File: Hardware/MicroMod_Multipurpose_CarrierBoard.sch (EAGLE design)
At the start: 100 parts, among them J11 microSD, J12 SPI, J14 I2C, J16 General GPIO, J17 I2C1, J18 DAC, J19 SPI1, J20 2.4" TFT, J3 JTAG, J5 UART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

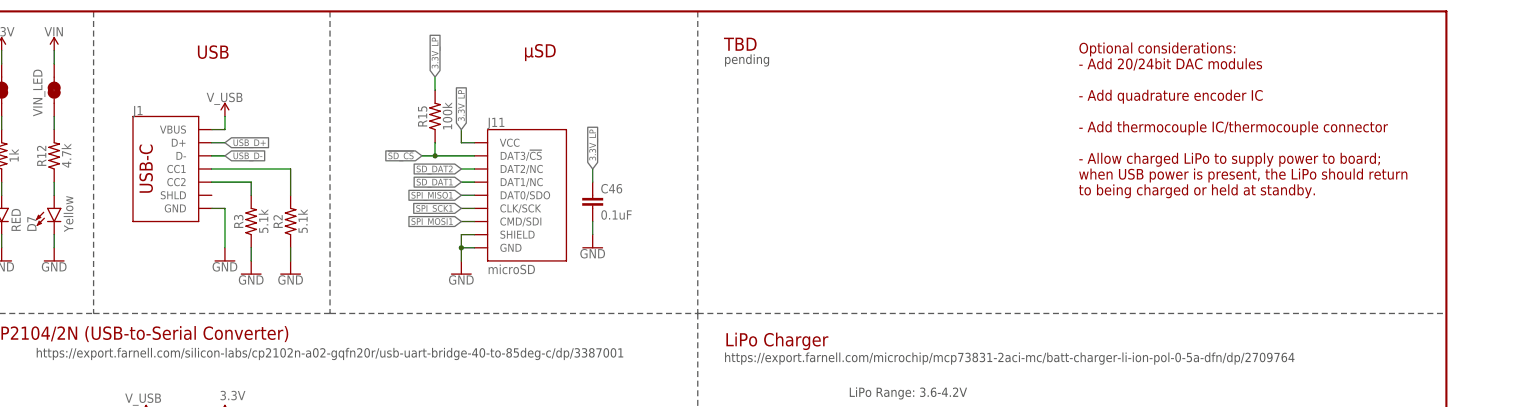
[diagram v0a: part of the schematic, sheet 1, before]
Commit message: Add ESD protection to USB data-lines
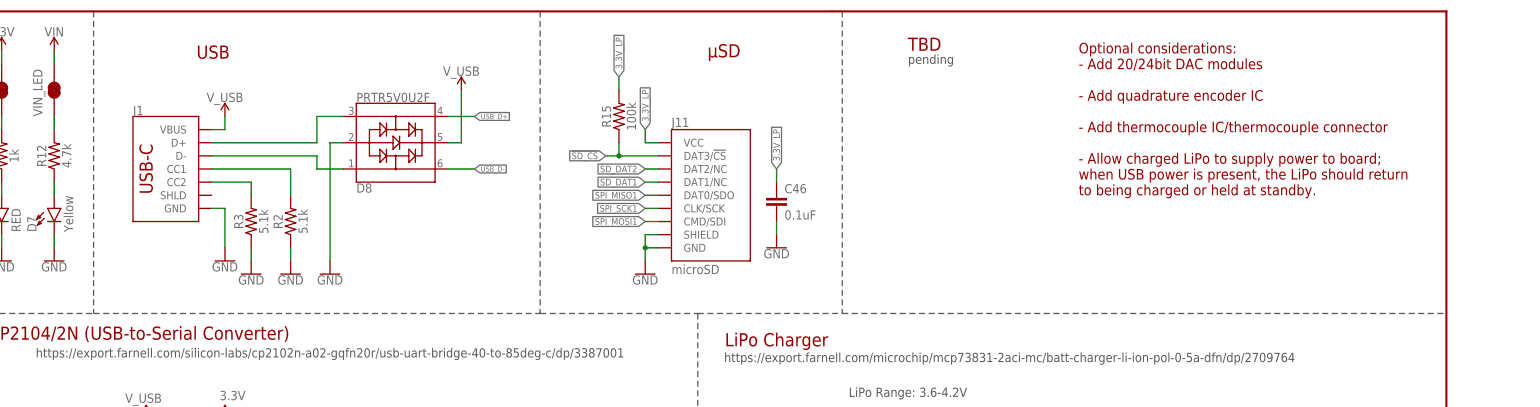
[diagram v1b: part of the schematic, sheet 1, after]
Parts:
- added D8: PRTR5V0U2F, SparkFun-IC-Power:PRTR5V0U2F
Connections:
- new net N$23: D8.1, J1.D-
- new net N$24: D8.3, J1.D+
- net GND: now also D8.2
- net USB_D+: now also D8.4; no longer J1.D+
- net USB_D-: now also D8.6; no longer J1.D-
- net V_USB: now also D8.5
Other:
- moved on the sheet: C46, J11, R15

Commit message: Minor correction
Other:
- note added: "Optional considerations: - Add 20/24bit ADC modules - Add quadrature encoder IC - Add thermocouple IC/thermocouple connector"
- note removed: "Optional considerations: - Add 20/24bit DAC modules - Add quadrature encoder IC - Add thermocouple IC/thermocouple connector - Allow charged LiPo to supply power to board; when USB power is present, the LiPo should return to being charged or held at standby."
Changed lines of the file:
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@@
 <wire x1="368.3" y1="106.68" x2="370.84" y2="106.68" width="0.2032" layer="97" style="longdash"/>
 <wire x1="370.84" y1="106.68" x2="370.84" y2="35.56" width="0.2032" layer="97" style="longdash"/>
-<text x="360.68" y="243.84" size="2.032" layer="94">Optional considerations:
-- Add 20/24bit DAC modules
+<text x="327.66" y="241.3" size="2.032" layer="94">Optional considerations:
+- Add 20/24bit ADC modules
 - Add quadrature encoder IC
 - Add thermocouple IC/thermocouple connector
-- Allow charged LiPo to supply power to board;
-when USB power is present, the LiPo should return
-to being charged or held at standby.</text>
+</text>
 <wire x1="137.16" y1="144.78" x2="132.08" y2="144.78" width="0.2032" layer="97" style="longdash"/>
 <wire x1="132.08" y1="144.78" x2="132.08" y2="124.46" width="0.2032" layer="97" style="longdash"/>

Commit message: Add header to program the ATMega328P & correct FTDI_DTR as pull_low to reset
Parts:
- added J15: AVR_SPI_PROG_3X2TESTPOINTS, SparkFun-Connectors:AVR_SPI_PROG_3X2TESTPOINTS
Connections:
- removed net FTDI_DTR: C11.1, J2.1
- new net !FTDI_DTR: C11.1, J15.5, J2.1
- net 3.3V: now also J15.2
- net GND: now also J15.6
- net I2C_SCL: now also J15.3
- net I2C_SDA: now also J15.4
- net SPI_MISO1: now also J15.1
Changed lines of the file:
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@@
 <part name="SUPPLY21" library="SparkFun-PowerSymbols" deviceset="V_USB" device=""/>
 <part name="GND1" library="SparkFun-PowerSymbols" deviceset="GND" device=""/>
+<part name="J15" library="SparkFun-Connectors" deviceset="AVR_SPI_PROG_3X2" device="TESTPOINTS"/>
+<part name="GND36" library="SparkFun-PowerSymbols" deviceset="GND" device=""/>
+<part name="SUPPLY22" library="SparkFun-PowerSymbols" deviceset="3.3V" device=""/>
 </parts>
 <sheets>
@@
 <attribute name="VALUE" x="215.9" y="228.346" size="1.778" layer="96" align="top-center"/>
 </instance>
+<instance part="J15" gate="G$1" x="109.22" y="208.28" smashed="yes">
+<attribute name="NAME" x="104.14" y="213.868" size="1.778" layer="95" font="vector"/>
+</instance>
+<instance part="GND36" gate="1" x="121.92" y="200.66" smashed="yes">
+<attribute name="VALUE" x="121.92" y="200.406" size="1.778" layer="96" font="vector" align="top-center"/>
+</instance>
+<instance part="SUPPLY22" gate="G$1" x="121.92" y="213.36" smashed="yes" rot="MR0">
+<attribute name="VALUE" x="121.92" y="216.154" size="1.778" layer="96" font="vector" rot="MR0" align="bottom-center"/>
+</instance>
 </instances>
 <busses>
@@
 <pinref part="GND1" gate="1" pin="GND"/>
 <wire x1="215.9" y1="254" x2="215.9" y2="231.14" width="0.1524" layer="91"/>
+</segment>
+<segment>
+<pinref part="J15" gate="G$1" pin="6"/>
+<wire x1="119.38" y1="205.74" x2="121.92" y2="205.74" width="0.1524" layer="91"/>
+<wire x1="121.92" y1="205.74" x2="121.92" y2="203.2" width="0.1524" layer="91"/>
+<pinref part="GND36" gate="1" pin="GND"/>
 </segment>
 </net>
@@
 <label x="363.22" y="124.46" size="1.27" layer="95" xref="yes"/>
 </segment>
+<segment>
+<pinref part="J15" gate="G$1" pin="2"/>
+<wire x1="119.38" y1="210.82" x2="121.92" y2="210.82" width="0.1524" layer="91"/>
+<wire x1="121.92" y1="210.82" x2="121.92" y2="213.36" width="0.1524" layer="91"/>
+<pinref part="SUPPLY22" gate="G$1" pin="3.3V"/>
+</segment>
 </net>
 <net name="V_USB" class="0">
@@
 </segment>
 </net>
-<net name="FTDI_DTR" class="0">
-<segment>
-<pinref part="J2" gate="G$1" pin="1"/>
-<wire x1="360.68" y1="132.08" x2="363.22" y2="132.08" width="0.1524" layer="91" style="longdash"/>
-<label x="363.22" y="132.08" size="1.27" layer="95" xref="yes"/>
-</segment>
-<segment>
-<pinref part="C11" gate="G$1" pin="1"/>
-<wire x1="20.32" y1="195.58" x2="17.78" y2="195.58" width="0.1524" layer="91"/>
-<label x="17.78" y="195.58" size="1.27" layer="95" font="vector" rot="R180" xref="yes"/>
-</segment>
-</net>
 <net name="FTDI_RXI" class="0">
 <segment>
@@
 <label x="101.6" y="182.88" size="1.27" layer="95" xref="yes"/>
 </segment>
+<segment>
+<pinref part="J15" gate="G$1" pin="3"/>
+<wire x1="101.6" y1="208.28" x2="99.06" y2="208.28" width="0.1524" layer="91"/>
+<label x="99.06" y="208.28" size="1.27" layer="95" font="vector" rot="R180" xref="yes"/>
+</segment>
 </net>
 <net name="I2C_SDA" class="0">
@@
 <wire x1="99.06" y1="185.42" x2="101.6" y2="185.42" width="0.1524" layer="91"/>
 <label x="101.6" y="185.42" size="1.27" layer="95" xref="yes"/>
+</segment>
+<segment>
+<pinref part="J15" gate="G$1" pin="4"/>
+<wire x1="119.38" y1="208.28" x2="121.92" y2="208.28" width="0.1524" layer="91"/>
+<label x="121.92" y="208.28" size="1.27" layer="95" font="vector" xref="yes"/>
 </segment>
 </net>
@@
 <wire x1="106.68" y1="15.24" x2="104.14" y2="15.24" width="0.1524" layer="91"/>
 <label x="104.14" y="15.24" size="1.27" layer="95" rot="R180" xref="yes"/>
+</segment>
+<segment>
+<pinref part="J15" gate="G$1" pin="1"/>
+<wire x1="101.6" y1="210.82" x2="99.06" y2="210.82" width="0.1524" layer="91"/>
+<label x="99.06" y="210.82" size="1.27" layer="95" font="vector" rot="R180" xref="yes"/>
 </segment>
 </net>
@@
 </segment>
 </net>
+<net name="!FTDI_DTR" class="0">
+<segment>
+<pinref part="J2" gate="G$1" pin="1"/>
+<wire x1="360.68" y1="132.08" x2="363.22" y2="132.08" width="0.1524" layer="91" style="longdash"/>
+<label x="363.22" y="132.08" size="1.27" layer="95" xref="yes"/>
+</segment>
+<segment>
+<pinref part="C11" gate="G$1" pin="1"/>
+<wire x1="20.32" y1="195.58" x2="17.78" y2="195.58" width="0.1524" layer="91"/>
+<label x="17.78" y="195.58" size="1.27" layer="95" font="vector" rot="R180" xref="yes"/>
+</segment>
+<segment>
+<pinref part="J15" gate="G$1" pin="5"/>
+<wire x1="101.6" y1="205.74" x2="99.06" y2="205.74" width="0.1524" layer="91"/>
+<label x="99.06" y="205.74" size="1.27" layer="95" font="vector" rot="R180" xref="yes"/>
+</segment>
+</net>

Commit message: Measure LiPO current using current-sense resistor and current-sense amp.
The voltage drop across the current-sense resistor is measured by the
comparator within the current-sense amplified, which is configured as
'ground referenced'; this means its output will be 0vdc when there is no
input voltage difference.

The current-sense opamp output is fed into the ADC input on the
ATMega328P.
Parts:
- added ISENSE1: Texas Instruments INA240A1PWR (TSSOP8), bsodmike-Eagle-Libraries:IN240ATSSOP8
- added R18: Vishay 3102723RL 0R1, rcl:R-EU_R5025
- J18: value DAC -> ADC
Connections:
- removed net ADC0: J18.2, U3.PC0(ADC0)
- removed net ADC1: J18.3, U3.PC1(ADC1)
- new net IN+: D3.C, ISENSE1.IN+, R18.1
- new net I_BATT: ISENSE1.OUT, U3.PC1(ADC1)
- net 3.3V: now also ISENSE1.VS
- net 5V: now also ISENSE1.IN-, R18.2; no longer D3.C
- net GND: now also ISENSE1.GND, ISENSE1.REF1, ISENSE1.REF2
- net I2C_SCL: no longer J15.3
- net I2C_SDA: no longer J15.4
- net SPI_MOSI1: now also J15.4
- net SPI_SCK1: now also J15.3
- net V_BATT: now also U3.PC0(ADC0)
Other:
- note added: "https://export.farnell.com/texas-instruments/ina240a1pwr/current-sense-amplifier-400khz/dp/3005360"
- note added: "https://export.farnell.com/vishay/wfmb2010r1000fea/res-0r1-2w-2010-metal-plate/dp/3102723RL"
- moved on the sheet: C3, C4, D2, D3, J4, J7, MEAS_BATT, R6, R7, U2
